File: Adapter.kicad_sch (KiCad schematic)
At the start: 0 parts

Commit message: VER2.1: переделал схему в один лист красиво
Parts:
- added C1, C2, C27, C28, C34, C35, C40, C41, C42, C5, C50, C51, C52, C53, C55, C6, C7, C75, C76, C77, C78, C8, C80, C84, C85, C88, C89: 2.2u, Capacitor_SMD:C_0805_2012Metric_Pad1.18x1.45mm_HandSolder, symbol Device:C_Small
- added C10, C11, C12, C13, C14, C15, C16, C17, C18, C19, C20, C3, C31, C36, C37, C38, C39, C4, C43, C44, C47, C48, C49, C9: 10u, Capacitor_SMD:C_1210_3225Metric_Pad1.33x2.70mm_HandSolder, symbol Device:C
- added C21, C23, C25, C57, C58, C63, C64, C69, C70: 0.1u, Capacitor_SMD:C_0805_2012Metric_Pad1.18x1.45mm_HandSolder, symbol Device:C_Small
- added C22, C24, C26: 10u, Capacitor_SMD:C_0805_2012Metric_Pad1.18x1.45mm_HandSolder, symbol Device:C_Small
- added C29, C56, C81: 10n, Capacitor_SMD:C_0805_2012Metric_Pad1.18x1.45mm_HandSolder, symbol Device:C_Small
- added C30, C45, C46, C54, C59, C60, C65, C66, C71, C72, C79, C82, C83, C86, C87: 56p, Capacitor_SMD:C_0805_2012Metric_Pad1.18x1.45mm_HandSolder, symbol Device:C_Small
- added C32: 10u, Capacitor_SMD:C_1210_3225Metric_Pad1.33x2.70mm_HandSolder, symbol Device:C_Small
- added C33: 22u, Capacitor_SMD:C_1210_3225Metric_Pad1.33x2.70mm_HandSolder, symbol Device:C_Small
- added C61, C62, C67, C68, C73, C74: 100p, Capacitor_SMD:C_0805_2012Metric_Pad1.18x1.45mm_HandSolder, symbol Device:C_Small
- added C90, C91, C92, C93, C94, C95: ~, Capacitor_SMD:C_0805_2012Metric_Pad1.18x1.45mm_HandSolder, symbol Device:C_Small
- added D1, D23, D25: SN74AHC1G08DBVR, Package_TO_SOT_SMD:SOT-23-5_HandSoldering, symbol Logic_My:MC74VHC1GT08DTT1G
- added D10, D16, D17, D18, D4, D43: WRA1215S-3WR2, Mornsun:WRA_S-3WR2, symbol Morsun:WRA1215S-3WR2
- added D11, D14, D15: YMC15S-1000A, Sensors_My:YMC15S-500A, symbol Sensors_My:YMC15S
- added D12, D27, D30: FLT, LED_SMD:LED_0805_2012Metric_Pad1.15x1.40mm_HandSolder, symbol Device:LED_Small
- added D13, D28, D49: RDY, LED_SMD:LED_0805_2012Metric_Pad1.15x1.40mm_HandSolder, symbol Device:LED_Small
- added D19, D29, D50: PWR, LED_SMD:LED_0805_2012Metric_Pad1.15x1.40mm_HandSolder, symbol Device:LED_Small
- added D2, D24, D26, D3, D5, D6, D7, D8, D9: ADM3485E, Package_SO:SOIC-8_3.9x4.9mm_P1.27mm, symbol Interface_My:ADM3485E_1
- added D20, D21, D22: ADM3485E, Package_SO:SOIC-8_3.9x4.9mm_P1.27mm, symbol Interface_My:ADM3485E
- added D31, D32, D37, D38, D44, D64: NSI6651ASC-DSWR, Package_SO:SOIC-16W_7.5x10.3mm_P1.27mm, symbol Driver_My:NSI6651
- added D33, D34, D39, D40, D45, D46: MMSZ5240B, Diode_SMD:D_SOD-123, symbol Device:D_Schottky_Small
- added D35, D36, D41, D42, D47, D48: MMSZ5232B, Diode_SMD:D_SOD-123, symbol Device:D_Zener_Small
- added D51: +5V, LED_SMD:LED_0805_2012Metric_Pad1.15x1.40mm_HandSolder, symbol Device:LED_Small
- added D58, D59, D60, D61, D62, D63: MURS160, Diode_SMD:D_SMA_Handsoldering, symbol Device:D_Small
- added J1: GD820HTX75P6HB, IGBT_Modul:GD820HTX75P6HB, symbol Connector_Generic:Conn_01x24
- added J3: Control_A, Connector_Molex:Molex_Micro-Fit_3.0_43045-1212_2x06_P3.00mm_Vertical, symbol Connector_Generic:Conn_02x06_Top_Bottom
- added J4: Control_C, Connector_Molex:Molex_Micro-Fit_3.0_43045-1212_2x06_P3.00mm_Vertical, symbol Connector_Generic:Conn_02x06_Top_Bottom
- added J5: Control_B, Connector_Molex:Molex_Micro-Fit_3.0_43045-1212_2x06_P3.00mm_Vertical, symbol Connector_Generic:Conn_02x06_Top_Bottom
- added L1, L2, L3, L4, L5, L6: 4.7u, Inductor_SMD:L_1812_4532Metric_Pad1.30x3.40mm_HandSolder, symbol Device:L
- added Q1, Q2, Q3: BC817, Package_TO_SOT_SMD:SOT-23, symbol Device:Q_NPN_BEC
- added R1, R10, R11, R12, R29, R30, R31, R58, R61, R62, R65, R73, R74, R77, R84, R85, R86, R9: 120, Resistor_SMD:R_0805_2012Metric_Pad1.20x1.40mm_HandSolder, symbol Device:R_Small
- added R100, R102, R98: 4.7k, Resistor_SMD:R_0805_2012Metric_Pad1.20x1.40mm_HandSolder, symbol Device:R_Small
- added R101, R109, R37, R38, R39, R40, R75, R76, R78, R82, R87, R88, R90, R94, R97, R99: 1k, Resistor_SMD:R_0805_2012Metric_Pad1.20x1.40mm_HandSolder, symbol Device:R_Small
- added R103, R104, R105, R106, R107, R108, R25, R26, R27, R56, R57, R59, R63, R64, R70: 10k, Resistor_SMD:R_0805_2012Metric_Pad1.20x1.40mm_HandSolder, symbol Device:R_Small
- added R110, R111, R112, R113, R114, R115, R116, R117, R118, R119, R120, R121: 560, Resistor_SMD:R_0805_2012Metric_Pad1.20x1.40mm_HandSolder, symbol Device:R_Small
- added R13, R14, R15, R16, R17, R18, R19, R20, R21, R22, R23, R24, R32, R33, R34, R35, R36, R41, R42, R43, R44, R45, R46, R47, R48, R49, R5, R50, R51, R52, R53, R54, R6, R66, R7, R8: 10, Resistor_SMD:R_1206_3216Metric_Pad1.30x1.75mm_HandSolder, symbol Device:R_Small
- added R2, R3, R4, R69, R71, R81, R83, R93, R95: 0, Resistor_SMD:R_0805_2012Metric_Pad1.20x1.40mm_HandSolder, symbol Device:R_Small
- added R28, R60, R72: 2.2k, Resistor_SMD:R_0805_2012Metric_Pad1.20x1.40mm_HandSolder, symbol Device:R_Small
- added R55, R89, R96: 3k, Resistor_SMD:R_0805_2012Metric_Pad1.20x1.40mm_HandSolder, symbol Device:R_Small
- added R67, R68, R79, R80, R91, R92: 2.4k, Resistor_SMD:R_0805_2012Metric_Pad1.20x1.40mm_HandSolder, symbol Device:R_Small
- added U1: K7805M-1000R3, DCDC_My:K78xxM-1000R3, symbol DCDC_My:K78xxM-1000R3
- added U11, U4, U8: LMV7219M5X/NOPB, Package_TO_SOT_SMD:SOT-23-5, symbol Comparator:LMV7219M5
- added U2, U3, U7: LM1117GS-5.0, Package_TO_SOT_SMD:SOT-223, symbol Regulator_Linear:LM1117-3.3
- added U5, U6, U9: ADuM1200AR, Package_SO:SOIC-8_3.9x4.9mm_P1.27mm, symbol Isolator:ADuM1200AR
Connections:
- new net: D38.4 (OUTH), R49.2, R50.2, R51.2
- new net: C54.2, R56.2, R60.1, U4.1, U6.2 (VIA)
- new net: C54.1, R56.1, R57.1, R59.2, U4.3 (+)
- new net: D20.4 (DI), U5.7 (VOA)
- new net: D30.2 (A), R90.1
- new net: D21.4 (DI), U6.7 (VOA)
- new net: D44.6 (OUTL), R36.1, R41.1, R42.1
- new net: C72.2, D37.14 (~{RST}), R86.2
- new net: C73.1, D37.2 (DESAT), D45.1 (K), R92.2
- new net: D37.4 (OUTH), R46.2, R47.2, R48.2
- new net: D37.6 (OUTL), R33.1, R34.1, R35.1
- new net: C19.1, D10.2 (Vin), L4.2
- new net: C59.2, D31.14 (~{RST}), R61.2
- new net: D36.1 (K), R71.1
- new net: R67.1, R71.2
- new net: C37.1, D43.2 (Vin), L2.2
- new net: C66.2, D64.14 (~{RST}), R74.2
- new net: C67.1, D39.1 (K), D64.2 (DESAT), R80.2
- new net: D64.4 (OUTH), R43.2, R44.2, R45.2
- new net: D64.6 (OUTL), R20.1, R21.1, R22.1
- new net: D32.4 (OUTH), R5.2, R6.2, R66.2
- new net: C79.2, R63.2, R72.1, U8.1, U9.2 (VIA)
- new net: D22.4 (DI), U9.7 (VOA)
- new net: C62.1, D31.2 (DESAT), D34.1 (K), R67.2
- new net: Q3.1 (B), R102.2
- new net: C71.2, D44.14 (~{RST}), R85.2
- new net: D32.6 (OUTL), R13.1, R7.1, R8.1
- new net: C9.1, D16.2 (Vin), L1.2
- new net: D31.6 (OUTL), R14.1, R15.1, R16.1
- new net: C39.1, D17.2 (Vin), L5.2
- new net: Q1.1 (B), R100.2
- new net: C65.2, D38.14 (~{RST}), R73.2
- new net: D31.4 (OUTH), R17.2, R18.2, R19.2
- new net: D36.2 (A), D59.2 (A)
- new net: D13.2 (A), R38.1
- new net: C48.1, D18.2 (Vin), L6.2
- new net: D49.2 (A), R94.1
- new net: Q2.1 (B), R98.2
- new net: D11.3 (Output), R2.1
- new net: D42.2 (A), D62.2 (A)
- new net: D44.4 (OUTH), R52.2, R53.2, R54.2
- new net: R91.1, R95.2
- new net: C74.1, D44.2 (DESAT), D46.1 (K), R91.2
- new net: C79.1, R63.1, R64.1, R70.2, U8.3 (+)
- new net: D25.4 (Y), D26.4 (DI)
- new net: C60.2, D32.14 (~{RST}), R62.2
- new net: C61.1, D32.2 (DESAT), D33.1 (K), R68.2
- new net: D41.1 (K), R81.1
- new net: D41.2 (A), D60.2 (A)
- new net: D50.2 (A), R96.1
- new net: D47.1 (K), R93.1
- new net: R92.1, R93.2
- new net: D51.2 (A), R97.1
- new net: C30.1, R25.1, R26.2, R27.1, U11.3 (+)
- new net: D29.2 (A), R89.1
- new net: D28.2 (A), R88.1
- new net: C68.1, D38.2 (DESAT), D40.1 (K), R79.2
- new net: D38.6 (OUTL), R23.1, R24.1, R32.1
- new net: D19.2 (A), R55.1
- new net: D15.3 (Output), R4.1
- new net: D12.2 (A), R37.1
- new net: C30.2, R27.2, R28.1, U11.1, U5.2 (VIA)
- new net: D1.4 (Y), D5.4 (DI)
- new net: D35.1 (K), R69.1
- new net: R68.1, R69.2
- new net: C13.1, D4.2 (Vin), L3.2
- new net: D47.2 (A), D61.2 (A)
- new net: D35.2 (A), D58.2 (A)
- new net: D48.2 (A), D63.2 (A)
- new net: D14.3 (Output), R3.1
- new net: D27.2 (A), R87.1
- new net: D23.4 (Y), D24.4 (DI)
- new net: D42.1 (K), R83.1
- new net: D48.1 (K), R95.1
- new net: R80.1, R81.2
- new net: R79.1, R83.2
- new net +15V: C12.1, C16.1, C18.1, C32.1, C38.1, C4.1, C47.1, J3.1 (Pin_1), J4.1 (Pin_1), J5.1 (Pin_1), L1.1, L2.1, L3.1, L4.1, L5.1, L6.1, R55.2, R89.2, R96.2, U1.1 (Vin)
- new net +15V_H1: C31.1, D32.5 (Vcc2), D43.6 (+Vo)
- new net +15V_H2: C11.1, D4.6 (+Vo), D64.5 (Vcc2)
- new net +15V_H3: C17.1, D10.6 (+Vo), D37.5 (Vcc2)
- new net +15V_L1: C3.1, D16.6 (+Vo), D31.5 (Vcc2)
- new net +15V_L2: C15.1, D17.6 (+Vo), D38.5 (Vcc2)
- new net +15V_L3: C44.1, D18.6 (+Vo), D44.5 (Vcc2)
- new net +5V: C1.1, C2.1, C21.1, C23.1, C25.1, C33.1, C34.1, C35.1, C41.1, C42.1, C5.1, C51.1, C53.1, C57.2, C58.2, C6.1, C63.2, C64.2, C69.2, C7.1, C70.2, C76.1, C78.1, C8.1, C84.1, C85.1, C88.1, C89.1, D1.5 (Vcc), D11.1 (+Vcc), D14.1 (+Vcc), D15.1 (+Vcc), D2.8 (VCC), D20.2 (RE), D20.3 (DE), D20.8 (VCC), D21.2 (RE), D21.3 (DE), D21.8 (VCC), D22.2 (RE), D22.3 (DE), D22.8 (VCC), D23.5 (Vcc), D24.2 (RE), D24.3 (DE), D24.8 (VCC), D25.5 (Vcc), D26.2 (RE), D26.3 (DE), D26.8 (VCC), D3.8 (VCC), D31.15 (Vcc1), D32.15 (Vcc1), D37.15 (Vcc1), D38.15 (Vcc1), D44.15 (Vcc1), D5.2 (RE), D5.3 (DE), D5.8 (VCC), D6.8 (VCC), D64.15 (Vcc1), D7.8 (VCC), D8.8 (VCC), D9.8 (VCC), R101.2, R109.2, R111.2, R113.2, R115.2, R117.2, R119.2, R121.2, R37.2, R39.2, R40.2, R75.2, R76.2, R78.2, R82.2, R87.2, R90.2, R97.2, R99.2, U1.3 (+Vo), U5.8 (VDD2), U6.8 (VDD2), U9.8 (VDD2)
- new net +5V_A: C75.1, C77.1, R64.2, U7.2 (VO), U8.5 (V+), U9.1 (VDD1)
- new net +5V_B: C50.1, C52.1, R57.2, U3.2 (VO), U4.5 (V+), U6.1 (VDD1)
- new net +5V_C: C28.1, C40.1, R25.2, U11.5 (V+), U2.2 (VO), U5.1 (VDD1)
- new net -15V_H1: C36.2, D32.1 (Vee2), D32.8 (Vee2), D43.8 (-Vo)
- new net -15V_H2: C14.2, D4.8 (-Vo), D64.1 (Vee2), D64.8 (Vee2)
- new net -15V_H3: C20.2, D10.8 (-Vo), D37.1 (Vee2), D37.8 (Vee2)
- new net -15V_L1: C10.2, C75.2, C77.2, C80.2, C81.2, D16.8 (-Vo), D31.1 (Vee2), D31.8 (Vee2), R70.1, U7.1 (GND), U8.2 (V-), U9.4 (GND1)
- new net -15V_L2: C43.2, C50.2, C52.2, C55.2, C56.2, D17.8 (-Vo), D38.1 (Vee2), D38.8 (Vee2), R59.1, U3.1 (GND), U4.2 (V-), U6.4 (GND1)
- new net -15V_L3: C27.2, C28.2, C29.2, C40.2, C49.2, D18.8 (-Vo), D44.1 (Vee2), D44.8 (Vee2), R26.1, U11.2 (V-), U2.1 (GND), U5.4 (GND1)
- new net C1: D58.1 (K), J1.1 (Pin_1)
- new net C2: D59.1 (K), J1.2 (Pin_2)
- new net C3: D60.1 (K), J1.9 (Pin_9)
- new net C4: D62.1 (K), J1.10 (Pin_10)
- new net C5: D61.1 (K), J1.17 (Pin_17)
- new net C6: D63.1 (K), J1.18 (Pin_18)
- new net Current_A_out: C22.1, J3.10 (Pin_10), R2.2
- new net Current_B_out: C24.1, J5.10 (Pin_10), R3.2
- new net Current_C_out: C26.1, J4.10 (Pin_10), R4.2
- new net E1: C31.2, C36.1, C61.2, C90.1, D32.3 (GND2), D33.2 (A), D43.7 (0V), J1.3 (Pin_3), R104.1
- new net E2: C10.1, C3.2, C62.2, C80.1, C91.1, D16.7 (0V), D31.3 (GND2), D34.2 (A), J1.4 (Pin_4), R103.1, U7.3 (VI)
- new net E3: C11.2, C14.1, C67.2, C92.1, D39.2 (A), D4.7 (0V), D64.3 (GND2), J1.11 (Pin_11), R105.1
- new net E4: C15.2, C43.1, C55.1, C68.2, C93.1, D17.7 (0V), D38.3 (GND2), D40.2 (A), J1.12 (Pin_12), R106.1, U3.3 (VI)
- new net E5: C17.2, C20.1, C73.2, C94.1, D10.7 (0V), D37.3 (GND2), D45.2 (A), J1.19 (Pin_19), R107.1
- new net E6: C27.1, C44.2, C49.1, C74.2, C95.1, D18.7 (0V), D44.3 (GND2), D46.2 (A), J1.20 (Pin_20), R108.1, U2.3 (VI)
- new net ERR_A_N: D5.7 (B), J3.12 (Pin_12), R1.1
- new net ERR_A_P: D5.6 (A), J3.6 (Pin_6), R1.2
- new net ERR_B_N: D24.7 (B), J5.12 (Pin_12), R77.1
- new net ERR_B_P: D24.6 (A), J5.6 (Pin_6), R77.2
- new net ERR_C_N: D26.7 (B), J4.12 (Pin_12), R84.1
- new net ERR_C_P: D26.6 (A), J4.6 (Pin_6), R84.2
- new net FLT_A: C45.1, D1.1 (B), D12.1 (K), D31.13 (~{FLT}), D32.13 (~{FLT}), R39.1
- new net FLT_B: C83.1, D23.1 (B), D27.1 (K), D38.13 (~{FLT}), D64.13 (~{FLT}), R76.1
- new net FLT_C: C87.1, D25.1 (B), D30.1 (K), D37.13 (~{FLT}), D44.13 (~{FLT}), R82.1
- new net G1: C90.2, D32.7 (CLAMP), J1.5 (Pin_5), R104.2, R13.2, R5.1, R6.1, R66.1, R7.2, R8.2
- new net G2: C91.2, D31.7 (CLAMP), J1.6 (Pin_6), R103.2, R14.2, R15.2, R16.2, R17.1, R18.1, R19.1
- new net G3: C92.2, D64.7 (CLAMP), J1.13 (Pin_13), R105.2, R20.2, R21.2, R22.2, R43.1, R44.1, R45.1
- new net G4: C93.2, D38.7 (CLAMP), J1.14 (Pin_14), R106.2, R23.2, R24.2, R32.2, R49.1, R50.1, R51.1
- new net G5: C94.2, D37.7 (CLAMP), J1.21 (Pin_21), R107.2, R33.2, R34.2, R35.2, R46.1, R47.1, R48.1
- new net G6: C95.2, D44.7 (CLAMP), J1.22 (Pin_22), R108.2, R36.2, R41.2, R42.2, R52.1, R53.1, R54.1
- new net GND: C1.2, C12.2, C13.2, C16.2, C18.2, C19.2, C2.2, C21.2, C22.2, C23.2, C24.2, C25.2, C26.2, C32.2, C33.2, C34.2, C35.2, C37.2, C38.2, C39.2, C4.2, C41.2, C42.2, C45.2, C46.2, C47.2, C48.2, C5.2, C51.2, C53.2, C57.1, C58.1, C59.1, C6.2, C60.1, C63.1, C64.1, C65.1, C66.1, C69.1, C7.2, C70.1, C71.1, C72.1, C76.2, C78.2, C8.2, C82.2, C83.2, C84.2, C85.2, C86.2, C87.2, C88.2, C89.2, C9.2, D1.3 (GND), D10.1 (GND), D11.2 (0V), D13.1 (K), D14.2 (0V), D15.2 (0V), D16.1 (GND), D17.1 (GND), D18.1 (GND), D19.1 (K), D2.2 (RE), D2.3 (DE), D2.5 (GND), D20.5 (GND), D21.5 (GND), D22.5 (GND), D23.3 (GND), D24.5 (GND), D25.3 (GND), D26.5 (GND), D28.1 (K), D29.1 (K), D3.2 (RE), D3.3 (DE), D3.5 (GND), D31.16 (TEST), D31.9 (GND1), D32.16 (TEST), D32.9 (GND1), D37.16 (TEST), D37.9 (GND1), D38.16 (TEST), D38.9 (GND1), D4.1 (GND), D43.1 (GND), D44.16 (TEST), D44.9 (GND1), D49.1 (K), D5.5 (GND), D50.1 (K), D51.1 (K), D6.2 (RE), D6.3 (DE), D6.5 (GND), D64.16 (TEST), D64.9 (GND1), D7.2 (RE), D7.3 (DE), D7.5 (GND), D8.2 (RE), D8.3 (DE), D8.5 (GND), D9.2 (RE), D9.3 (DE), D9.5 (GND), J3.7 (Pin_7), J4.7 (Pin_7), J5.7 (Pin_7), Q1.2 (E), Q2.2 (E), Q3.2 (E), R110.1, R112.1, R114.1, R116.1, R118.1, R120.1, U1.2 (GND), U5.5 (GND2), U6.5 (GND2), U9.5 (GND2)
- new net PWM1_H_N: D2.7 (B), J3.5 (Pin_5), R112.2, R31.1
- new net PWM1_H_P: D2.6 (A), J3.11 (Pin_11), R113.1, R31.2
- new net PWM1_L_N: D3.7 (B), J3.2 (Pin_2), R110.2, R30.1
- new net PWM1_L_P: D3.6 (A), J3.8 (Pin_8), R111.1, R30.2
- new net PWM2_H_N: D9.7 (B), J5.5 (Pin_5), R10.1, R116.2
- new net PWM2_H_P: D9.6 (A), J5.11 (Pin_11), R10.2, R117.1
- new net PWM2_L_N: D8.7 (B), J5.2 (Pin_2), R114.2, R9.1
- new net PWM2_L_P: D8.6 (A), J5.8 (Pin_8), R115.1, R9.2
- new net PWM3_H_N: D7.7 (B), J4.5 (Pin_5), R12.1, R120.2
- new net PWM3_H_P: D7.6 (A), J4.11 (Pin_11), R12.2, R121.1
- new net PWM3_L_N: D6.7 (B), J4.2 (Pin_2), R11.1, R118.2
- new net PWM3_L_P: D6.6 (A), J4.8 (Pin_8), R11.2, R119.1
- new net PWM_H1: D2.1 (RO), D31.11 (IN-), D32.10 (IN+)
- new net PWM_H2: D38.11 (IN-), D64.10 (IN+), D9.1 (RO)
- new net PWM_H3: D37.10 (IN+), D44.11 (IN-), D7.1 (RO)
- new net PWM_L1: D3.1 (RO), D31.10 (IN+), D32.11 (IN-)
- new net PWM_L2: D38.10 (IN+), D64.11 (IN-), D8.1 (RO)
- new net PWM_L3: D37.11 (IN-), D44.10 (IN+), D6.1 (RO)
- new net RDY_A: C46.1, D1.2 (A), D31.12 (RDY), D32.12 (RDY), R38.2, R40.1
- new net RDY_B: C82.1, D23.2 (A), D38.12 (RDY), D64.12 (RDY), R75.1, R88.2
- new net RDY_C: C86.1, D25.2 (A), D37.12 (RDY), D44.12 (RDY), R78.1, R94.2
- new net T1: C81.1, J1.7 (Pin_7), U8.4 (-)
- new net T2: J1.8 (Pin_8), R72.2
- new net T3: C56.1, J1.15 (Pin_15), U4.4 (-)
- new net T4: J1.16 (Pin_16), R60.2
- new net T5: C29.1, J1.23 (Pin_23), U11.4 (-)
- new net T6: J1.24 (Pin_24), R28.2
- new net Temp_A_N: D22.7 (B), J3.9 (Pin_9), R65.1
- new net Temp_A_P: D22.6 (A), J3.3 (Pin_3), R65.2
- new net Temp_B_N: D21.7 (B), J5.9 (Pin_9), R58.1
- new net Temp_B_P: D21.6 (A), J5.3 (Pin_3), R58.2
- new net Temp_C_N: D20.7 (B), J4.9 (Pin_9), R29.1
- new net Temp_C_P: D20.6 (A), J4.3 (Pin_3), R29.2
- new net ~{RST_A}: Q2.3 (C), R61.1, R62.1, R99.1
- new net ~{RST_B}: Q1.3 (C), R101.1, R73.1, R74.1
- new net ~{RST_C}: Q3.3 (C), R109.1, R85.1, R86.1
- new net ~{RST}: J3.4 (Pin_4), J4.4 (Pin_4), J5.4 (Pin_4), R100.1, R102.1, R98.1
- no-connect marks 0 -> 24
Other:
- removed sheet Connectors
- removed sheet Current_Sensors
- removed sheet Driver_1
- removed sheet Driver_2
- removed sheet Driver_3
- removed sheet Fault1
- removed sheet Logic_Pritection
- removed sheet Logic_Protection2
- removed sheet Logic_Protection3
- removed sheet NTC_Handler
- removed sheet Power_Supply_1
- removed sheet Power_Supply_2
- removed sheet Power_Supply_3
- removed sheet SupplyPower_5V
- note added: "Датчик тока фазы А"
- note added: "Датчик тока фазы В"
- note added: "Датчик тока фазы С"
- note added: "Драйвер верхнего ключа фазы B"
- note added: "Драйвер верхнего ключа фазы C"
- note added: "Драйвер верхнего ключа фазы А"
- note added: "Драйвер нижнего ключа фазы B"
- note added: "Драйвер нижнего ключа фазы C"
- note added: "Драйвер нижнего ключа фазы А"
- note added: "Индикация A"
- note added: "Индикация B"
- note added: "Индикация C"
- note added: "НВЦТ.EVP150-2-1.2000.120"
- note added: "Ошибка фазы B"
- note added: "Ошибка фазы C"
- note added: "Ошибка фазы А"
- note added: "Питание +5В"
- note added: "Питание драйверов"
- note added: "Преобразование температуры фазы A"
- note added: "Преобразование температуры фазы B"
- note added: "Преобразование температуры фазы C"
- note added: "Разъем фазы А"
- note added: "Разъем фазы В"
- note added: "Разъем фазы С"
- note added: "Сброс ошибки фазы А"
- note added: "Сброс ошибки фазы В"
- note added: "Сброс ошибки фазы С"
- note added: "Схема электрическая принципиальная"
- note added: "Трехфазный модуль"
- note added: "ШИМ фазы А"
- note added: "ШИМ фазы В"
- note added: "ШИМ фазы С"

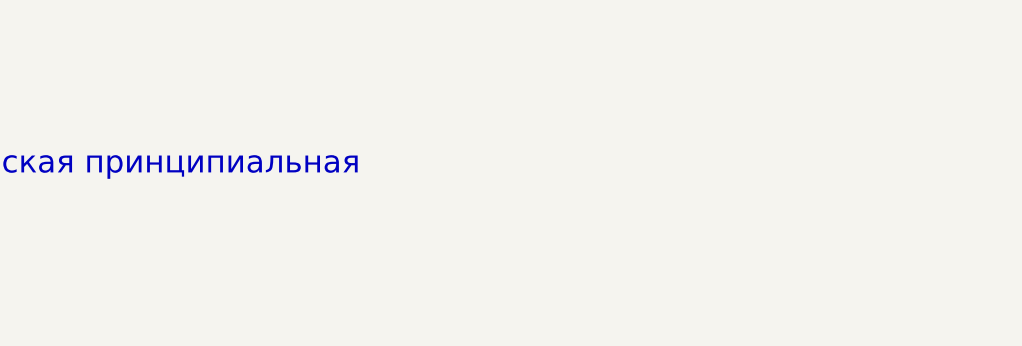
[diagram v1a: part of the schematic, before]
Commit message: VER2.1: исправил Э3
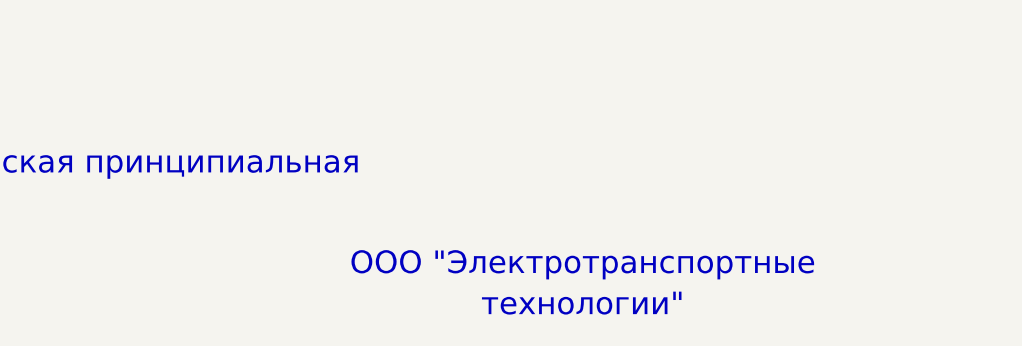
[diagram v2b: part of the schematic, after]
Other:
- note added: "ООО "Электротранспортные"
- note added: "технологии""
- company: ООО "Электротранспортные технологии" -> (none)
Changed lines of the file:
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@@
 	(title_block
 		(title "Плата драйверов модуля фазных обмоток")
-		(company "ООО \"Электротранспортные технологии\"")
 		(comment 1 "НВЦТ.EVP150-2-1.2000.120 Э3")
 		(comment 2 "Филатов А.С.")
@@
 		)
 	)
+	(text "ООО \"Электротранспортные"
+		(exclude_from_sim no)
+		(at 811.276 579.628 0)
+		(effects
+			(font
+				(size 2.5 2.5)
+			)
+		)
+	)
 	(text "Драйвер верхнего ключа фазы А"
 		(exclude_from_sim no)
@@
 			)
 		)
+	)
+	(text "технологии\""
+		(exclude_from_sim no)
+		(at 811.276 584.2 0)
+		(effects
+			(font
+				(size 2.5 2.5)
+			)
+		)

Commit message: VER2.1: исправил Э3 еще раз
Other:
- note added: "1. Перечень элементов см. НВЦТ.EVP150-2-1.2000.120 ПЭ3."
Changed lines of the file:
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@@
+		)
+	)
+	(text "1. Перечень элементов см. НВЦТ.EVP150-2-1.2000.120 ПЭ3."
+		(exclude_from_sim no)
+		(at 710.946 513.08 0)
+		(effects
+			(font
+				(size 3.5 3.5)
+			)
 		)
 	)
